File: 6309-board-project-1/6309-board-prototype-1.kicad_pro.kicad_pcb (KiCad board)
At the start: 2 copper layers, 23 parts, among them J1 PWR, J2 FTDI, SW1 SW_Push, U1 HD63C09, U2 62256, U3 28C256, U4 16C550, U5 74HCT04, U6 74HCT32, U7 74HCT30, X1 12MHz, X2 1.8432MHz

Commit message: changed rom, added correct switch, added a million footprints
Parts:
- removed C10: 100nF, Capacitor_THT:C_Disc_D5.0mm_W2.5mm_P5.00mm
- removed R1: 1K, Resistor_THT:R_Axial_DIN0207_L6.3mm_D2.5mm_P5.08mm_Vertical
- added C11: 47pF, Capacitor_THT:C_Disc_D5.0mm_W2.5mm_P5.00mm, F.Cu at (17.0, 89.0)
- added C12: 18pF, Custom:CAP_C317_KEM, F.Cu at (81.1, 69.0)
- added C13: 1uF, Custom:CAP_C330C_MR_X7R_KEM, F.Cu at (76.4, 92.0)
- added C14: 0.1uF, Custom:CAP_C320C_MR_X7R_KEM, F.Cu at (57.0, 51.2)
- added C15: 0.01uF, Custom:CAP_C315C_MR_X7R_KEM, F.Cu at (31.0, 89.1)
- added C16: 0.1uF, Custom:CAP_C320C_MR_X7R_KEM, F.Cu at (57.0, 56.1)
- added R2: 1.5k, Resistor_THT:R_Axial_DIN0207_L6.3mm_D2.5mm_P5.08mm_Vertical, F.Cu at (82.1, 17.0)
- added R3: 1M, Resistor_THT:R_Axial_DIN0207_L6.3mm_D2.5mm_P5.08mm_Vertical, F.Cu at (82.1, 21.1)
- added R4: 100K, Resistor_THT:R_Axial_DIN0207_L6.3mm_D2.5mm_P5.08mm_Vertical, F.Cu at (82.1, 25.1)
- added R5: 100K, Resistor_THT:R_Axial_DIN0207_L6.3mm_D2.5mm_P5.08mm_Vertical, F.Cu at (82.1, 29.2)
- added R6: 100K, Resistor_THT:R_Axial_DIN0207_L6.3mm_D2.5mm_P5.08mm_Vertical, F.Cu at (82.1, 33.2)
- added R7: 100K, Resistor_THT:R_Axial_DIN0207_L6.3mm_D2.5mm_P5.08mm_Vertical, F.Cu at (82.1, 37.3)
- added R8: 100K, Resistor_THT:R_Axial_DIN0207_L6.3mm_D2.5mm_P5.08mm_Vertical, F.Cu at (82.1, 41.3)
- added R9: 100K, Resistor_THT:R_Axial_DIN0207_L6.3mm_D2.5mm_P5.08mm_Vertical, F.Cu at (82.1, 45.4)
- C1, C2, C3, C4, C5, C6: value 0.01uF -> 0.1uF; footprint Capacitor_THT:C_Disc_D5.0mm_W2.5mm_P2.50mm -> Custom:CAP_C320C_MR_X7R_KEM
- C7: value 0.01uf -> 0.1uF; footprint Capacitor_THT:C_Disc_D5.0mm_W2.5mm_P2.50mm -> Custom:CAP_C320C_MR_X7R_KEM
- C8, C9: value 20pF -> 24pF; footprint Capacitor_THT:C_Disc_D5.0mm_W2.5mm_P5.00mm -> Custom:CAP_C317_KEM
- SW1: value SW_Push -> B3F-1000; footprint Button_Switch_THT:SW_PUSH_6mm_H5mm -> Custom:SW_B3F-1000_OMR
- U1: value HD63C09 -> 63C09
- U3: value 28C256 -> 39FS010; footprint Package_DIP:DIP-28_W7.62mm_Socket -> Package_DIP:DIP-32_W15.24mm
- X2: value 1.8432MHz -> 1.8432 MHz; footprint Oscillator:Oscillator_DIP-8 -> Crystal:Crystal_HC49-U_Vertical
- moved U2 42.9 mm to (56.3, 60.6)
- moved J1 42.5 mm to (25.9, 89.3)
- moved C1 37.5 mm to (57.0, 17.4)
- moved C2 36.7 mm to (57.0, 22.2)
- moved C3 35.9 mm to (57.0, 27.1)
- moved C4 35.1 mm to (57.0, 31.9)
- moved C5 34.3 mm to (57.0, 36.7)
- moved C6 33.6 mm to (57.0, 41.6)
- moved C7 32.8 mm to (57.0, 46.4)
- moved X2 25.9 mm to (77.7, 85.8)
- moved SW1 25.8 mm to (81.6, 50.7)
- moved C8 16.5 mm to (81.1, 60.6)
- moved C9 16.5 mm to (81.1, 64.8)
- moved J2 15.6 mm to (76.0, 60.8)
- moved U3 12.4 mm to (63.2, 17.1)
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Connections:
- C6 pad 1: Net-(U6E-VCC) -> +5V
- SW1 pad 1: /!RESET -> +5V
- SW1 pad 2: GND -> (no net)
- U1 pad 2: +5V -> Net-(U1-MRDY)
- U1 pad 3: Net-(U1-~{IRQ}) -> /!RESET
- U1 pad 33: +5V -> Net-(U1-MRDY)
- U1 pad 36: +5V -> Net-(U1-MRDY)
- U1 pad 4: +5V -> Net-(U1-MRDY)
- U1 pad 40: +5V -> Net-(U1-MRDY)
- U3 pad 1: /A14 -> unconnected-(U3-NC-Pad1)
- U3 pad 10: /A0 -> /A2
- U3 pad 11: /D0 -> /A1
- U3 pad 12: /D1 -> /A0
- U3 pad 13: /D2 -> /D0
- U3 pad 14: GND -> /D1
- U3 pad 15: /D3 -> /D2
- U3 pad 16: /D4 -> GND
- U3 pad 17: /D5 -> /D3
- U3 pad 18: /D6 -> /D4
- U3 pad 19: /D7 -> /D5
- U3 pad 2: /A12 -> Net-(U3-A15)
- U3 pad 20: /!A15 -> /D6
- U3 pad 21: /A10 -> /D7
- U3 pad 23: /A11 -> /A10
- U3 pad 24: /A9 -> /!A15
- U3 pad 25: /A8 -> /A11
- U3 pad 26: /A13 -> /A9
- U3 pad 27: /R/!W -> /A8
- U3 pad 28: +5V -> /A13
- U3 pad 3: /A7 -> Net-(U3-A15)
- U3 pad 4: /A6 -> /A12
- U3 pad 5: /A5 -> /A7
- U3 pad 6: /A4 -> /A6
- U3 pad 7: /A3 -> /A5
- U3 pad 8: /A2 -> /A4
- U3 pad 9: /A1 -> /A3
- U4 pad 12: +5V -> Net-(U4-CS0)
- U4 pad 13: +5V -> Net-(U4-CS0)
- U4 pad 17: unconnected-(U4-XOUT-Pad17) -> Net-(U4-XOUT)
- U4 pad 19: GND -> Net-(U4-WR)
- U4 pad 21: +5V -> Net-(U4-CS0)
- U4 pad 25: GND -> Net-(U4-WR)
- U4 pad 37: GND -> Net-(U4-~{DCD})
- U4 pad 38: GND -> Net-(U4-~{DCD})
- U5 pad 4: Net-(U1-~{IRQ}) -> /!RESET
- U6 pad 14: Net-(U6E-VCC) -> +5V
- X2 pad 1: +5V -> Net-(U4-XIN)

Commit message: fixed schematic, started pcb
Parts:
- U4: value 16C550 -> 16550
- moved C9 66.5 mm to (35.0, 16.8), turned to 90 degrees
- moved X1 66.0 mm to (40.0, 25.0), turned to 180 degrees
- moved R2 64.4 mm to (146.4, 18.2)
- moved R3 64.4 mm to (146.4, 22.2)
- moved R4 64.4 mm to (146.4, 26.3)
- moved R5 64.4 mm to (146.4, 30.4)
- moved R6 64.4 mm to (146.4, 34.4)
- moved R7 64.4 mm to (146.4, 38.5)
- moved R8 64.4 mm to (146.4, 42.5)
- moved R9 64.4 mm to (146.4, 46.5)
- moved SW1 64.4 mm to (146.0, 51.9)
- moved C11 64.0 mm to (78.5, 106.8)
- moved C15 64.0 mm to (92.5, 106.9)
- moved U5 64.0 mm to (79.0, 87.4)
- moved U6 64.0 mm to (90.7, 87.4)
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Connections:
- U1 pad 3: /!RESET -> Net-(U1-~{IRQ})
- U5 pad 4: /!RESET -> Net-(U1-~{IRQ})
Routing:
- net GND: track 0.00 -> 49.0 mm
- net Net-(U1-EXTAL): track 0.00 -> 24.6 mm
- net +5V: track 0.00 -> 22.6 mm
- net Net-(U1-XTAL): track 0.00 -> 20.0 mm

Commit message: pcb work
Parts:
- moved C14 137.5 mm to (244.5, 51.5)
- moved C16 137.5 mm to (244.5, 56.3)
- moved C5 137.5 mm to (244.5, 37.0)
- moved C6 137.5 mm to (244.5, 41.8)
- moved C7 137.5 mm to (244.5, 46.6)
- moved C12 106.6 mm to (249.0, 89.7)
- moved J2 106.6 mm to (243.9, 81.5)
- moved R2 106.6 mm to (252.9, 22.4)
- moved R3 106.6 mm to (252.9, 26.4)
- moved R4 106.6 mm to (252.9, 30.4)
- moved R5 106.6 mm to (252.9, 34.5)
- moved R6 106.6 mm to (252.9, 38.5)
- moved R7 106.6 mm to (252.9, 42.6)
- moved R8 106.6 mm to (252.9, 46.6)
- moved R9 106.6 mm to (252.9, 50.7)
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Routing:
- net /A8: track 0.00 -> 117.5 mm
- net /A12: track 0.00 -> 113.2 mm
- net /A14: track 0.00 -> 109.2 mm
- net /A13: track 0.00 -> 104.8 mm
- net /A9: track 0.00 -> 103.9 mm
- net /A11: track 0.00 -> 101.8 mm
- net /A7: track 0.00 -> 98.8 mm
- net /A10: track 0.00 -> 97.4 mm
- net /A6: track 0.00 -> 93.4 mm
- net GND: track 49.0 -> 138.9 mm
- net /D7: track 0.00 -> 88.6 mm
- net /A5: track 0.00 -> 87.5 mm
- net /D6: track 0.00 -> 83.3 mm
- net /A4: track 0.00 -> 82.0 mm
- net /A2: track 0.00 -> 80.0 mm
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
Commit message: schematic work
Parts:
- moved C5 210.1 mm to (43.5, 98.4), turned to 90 degrees
- moved C15 204.3 mm to (273.1, 34.3)
- moved J1 204.3 mm to (268.0, 34.5)
- moved C6 203.8 mm to (42.0, 65.0), turned to 90 degrees
- moved C7 202.4 mm to (42.5, 33.5), turned to 90 degrees
- moved J2 163.7 mm to (92.2, 20.0), turned to -90 degrees
- moved C12 150.8 mm to (116.4, 18.0), turned to 90 degrees
- moved R3 136.4 mm to (116.6, 27.5)
- moved R2 134.3 mm to (120.4, 44.2), turned to -90 degrees
- moved C13 128.5 mm to (262.3, 140.7)
- moved C11 122.7 mm to (121.9, 20.5), turned to 90 degrees
- moved U7 105.3 mm to (35.0, 39.9)
- moved X1 92.6 mm to (121.0, 70.0)
- moved C9 92.0 mm to (116.5, 59.4)
- moved C8 91.1 mm to (120.5, 59.4)
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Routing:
- net /A8: track 117.5 -> 0.00 mm
- net /A12: track 113.2 -> 0.00 mm
- net /A14: track 109.2 -> 0.00 mm
- net /A13: track 104.8 -> 0.00 mm
- net /A9: track 103.9 -> 0.00 mm
- net /A11: track 101.8 -> 0.00 mm
- net /A7: track 98.8 -> 0.00 mm
- net /A10: track 97.4 -> 0.00 mm
- net /A6: track 93.4 -> 0.00 mm
- net /D7: track 88.6 -> 0.00 mm
- net /A5: track 87.5 -> 0.00 mm
- net /D6: track 83.3 -> 0.00 mm
- net /A4: track 82.0 -> 0.00 mm
- net /A3: track 78.7 -> 0.00 mm
- net /D5: track 77.7 -> 0.00 mm
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
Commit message: pcb work, again
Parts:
- moved C15 257.3 mm to (36.0, 134.0)
- moved J1 250.3 mm to (36.0, 128.5), turned to 90 degrees
- moved C13 227.4 mm to (34.9, 146.0)
- moved C14 210.5 mm to (36.1, 139.5)
- moved C11 75.4 mm to (46.5, 19.5), turned to 180 degrees
- moved C12 72.7 mm to (44.0, 25.0), turned to 180 degrees
- moved R3 61.6 mm to (55.0, 24.8), turned to 90 degrees
- moved R2 58.9 mm to (64.0, 27.2)
- moved X2 50.0 mm to (69.0, 20.0), turned to 180 degrees
- moved C3 3.57 mm to (71.6, 95.5)
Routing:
- net /D5: track 0.00 -> 97.8 mm
- net /D3: track 0.00 -> 92.5 mm
- net /D2: track 0.00 -> 89.2 mm
- net /D6: track 0.00 -> 88.6 mm
- net /D4: track 0.00 -> 86.8 mm
- net /D1: track 0.00 -> 85.6 mm
- net /D0: track 0.00 -> 82.1 mm
- net /D7: track 0.00 -> 80.5 mm
- net Net-(U4-XOUT): track 57.1 -> 7.38 mm
- net GND: track 76.6 -> 113.2 mm
- net +5V: track 15.4 -> 49.8 mm
- net /A4: track 0.00 -> 31.9 mm
- net /A2: track 22.8 -> 54.4 mm
- net /A5: track 0.00 -> 31.7 mm
- net /A3: track 0.00 -> 31.7 mm
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
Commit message: schematic work once again, getting close
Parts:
- moved R7 219.5 mm to (53.8, 37.9), turned to -90 degrees
- moved R5 198.0 mm to (75.5, 31.3), turned to 90 degrees
- moved R8 196.6 mm to (71.6, 99.5), turned to 180 degrees
- moved R4 159.2 mm to (109.0, 64.1), turned to 90 degrees
- moved R6 154.5 mm to (113.5, 85.7), turned to -90 degrees
- moved SW1 133.1 mm to (148.2, 40.1)
- moved C16 122.1 mm to (151.0, 53.4), turned to 90 degrees
- moved R9 119.4 mm to (155.7, 53.2)
- moved C3 51.3 mm to (68.4, 146.8), turned to 180 degrees
- moved C4 5.51 mm to (105.2, 102.5), turned to 180 degrees
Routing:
- net GND: track 113.2 -> 311.1 mm
- net +5V: track 49.8 -> 203.0 mm
- net /R/!W: track 0.00 -> 113.4 mm
- net /A3: track 31.7 -> 119.7 mm
- net /A4: track 31.9 -> 112.9 mm
- net /A5: track 31.7 -> 106.2 mm
- net /A0: track 54.4 -> 123.3 mm
- net /A6: track 31.7 -> 99.7 mm
- net /A13: track 31.7 -> 99.1 mm
- net /A1: track 54.4 -> 119.7 mm
- net /A10: track 31.7 -> 94.7 mm, vias 0 -> 1
- net /A2: track 54.4 -> 116.2 mm
- net /A7: track 31.7 -> 92.5 mm
- net /D1: track 85.6 -> 144.1 mm, vias 0 -> 1
- net /D7: track 80.5 -> 138.9 mm, vias 0 -> 1
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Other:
- rule pad_to_mask_clearance: 0 -> 0.0762

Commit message: schematic work
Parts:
- moved R9 54.3 mm to (107.2, 28.6), turned to 90 degrees
- moved C16 41.7 mm to (116.5, 30.0), turned to 180 degrees
- moved SW1 41.6 mm to (111.7, 20.2)
- moved R8 12.4 mm to (60.0, 94.9), turned to -90 degrees
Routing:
- net +5V: track 203.0 -> 322.1 mm
- net /!RESET: track 0.00 -> 90.0 mm
- net /A11: track 31.7 -> 89.7 mm
- net Net-(U4-MR): track 0.00 -> 39.5 mm
- net Net-(U4-INTR): track 0.00 -> 26.1 mm
- net GND: track 311.1 -> 317.1 mm
- net /A13: track 99.1 -> 94.4 mm
- net Net-(U4-~{DCD}): track 11.9 -> 15.7 mm
- net Net-(U3-A15): track 12.5 -> 10.1 mm
- net /D1: track 144.1 -> 143.1 mm
- net /D3: track 148.3 -> 147.4 mm
- net /D7: track 138.9 -> 138.0 mm
- net /D6: track 146.9 -> 146.1 mm
- net /D0: track 140.4 -> 139.6 mm
- net /D2: track 147.6 -> 146.7 mm
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
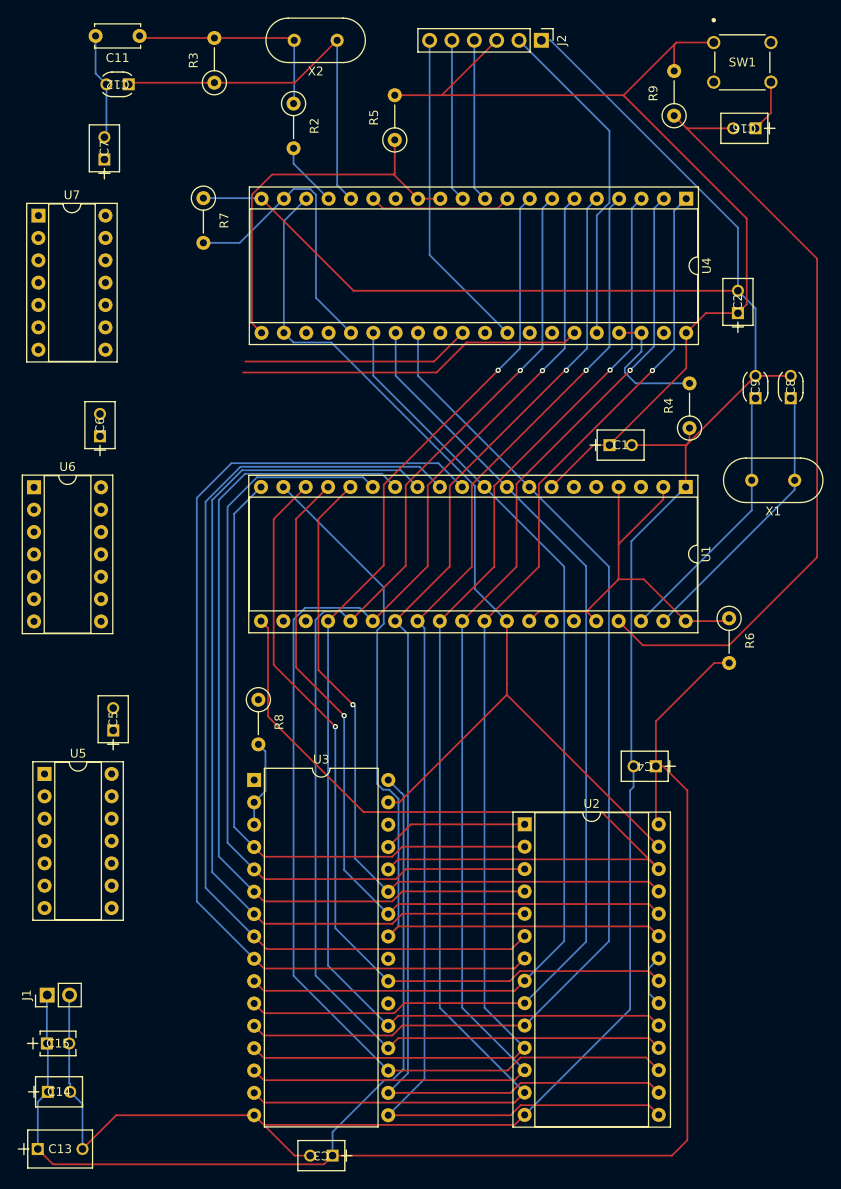
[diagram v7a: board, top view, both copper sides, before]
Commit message: fixed CTS/RTS and doubled width of power traces
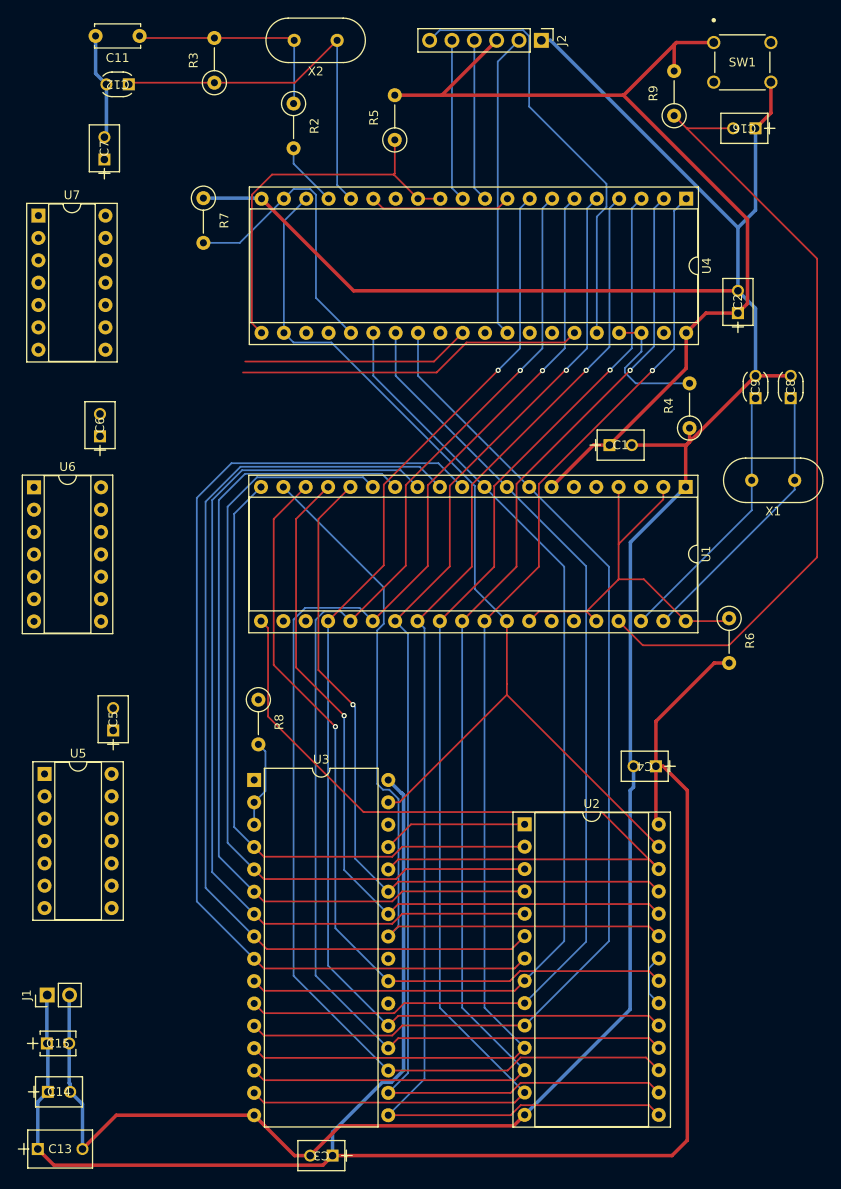
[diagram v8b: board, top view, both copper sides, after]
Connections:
- U4 pad 32: /RTS -> /CTS
- U4 pad 36: /CTS -> /RTS
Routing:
- net /RTS: track 36.9 -> 49.9 mm
- net GND: track 317.1 -> 325.5 mm
- net /CTS: track 38.1 -> 34.7 mm
